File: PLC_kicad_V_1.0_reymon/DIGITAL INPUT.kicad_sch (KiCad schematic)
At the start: 9 parts, among them U1 FODM214A

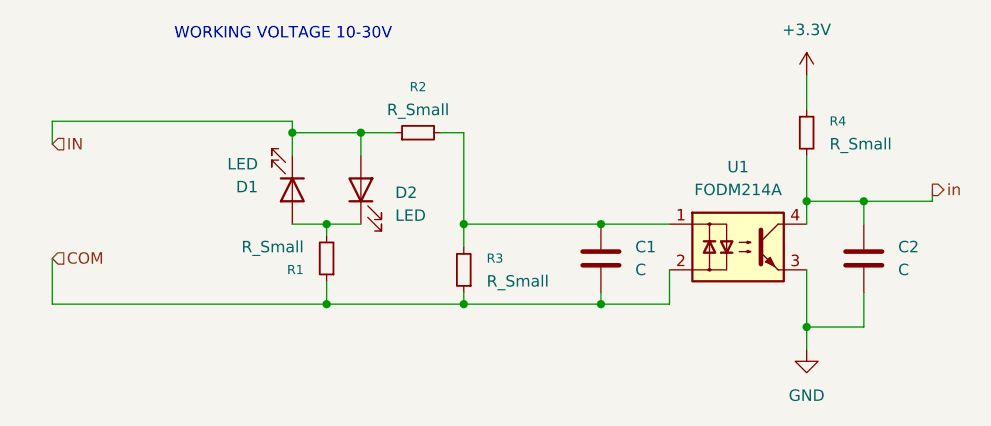
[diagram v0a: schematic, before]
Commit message: fotos de circuitos investigado, diagramas de bloque de estos circuitos<aun en proceso>,se anadio zip y lck al gitignore, y subir pcb_mezzanine con ajuste de tamano y plano de tierra<aun en proceso de configuracion de stack up y demas>
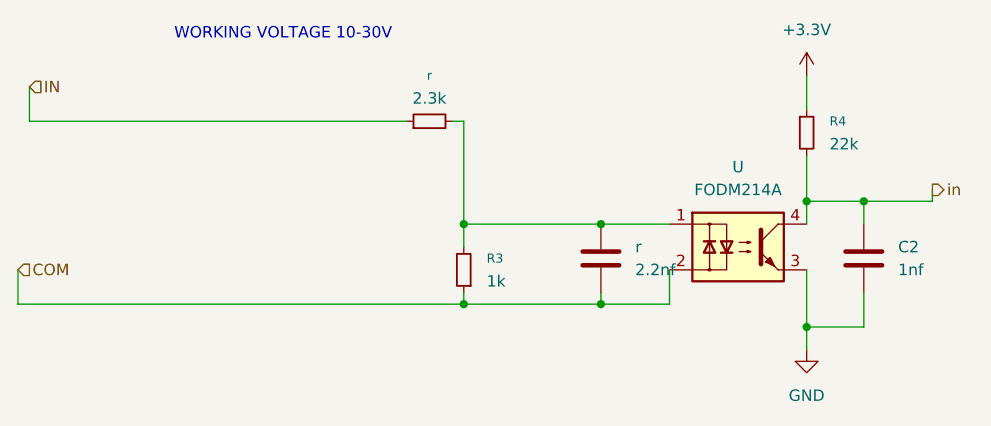
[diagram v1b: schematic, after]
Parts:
- removed D1, D2: LED, symbol Device:LED
- removed R1: R_Small, symbol Device:R_Small
- C2: value C -> 1nf
- R3: value R_Small -> 1k
- R4: value R_Small -> 22k
- r: renamed from C1; value C -> 2.2nf
- r: renamed from R2; value R_Small -> 2.3k
- renumbered U1 to U
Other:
- moved on the sheet: r
